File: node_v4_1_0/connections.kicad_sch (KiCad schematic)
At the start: 13 parts, among them J1 Conn_01x02_Pin, J4 Conn_02x08_Odd_Even, J5 Conn_02x02_Odd_Even, J6 GNSS_ANT, J7 RF_ANT, J8 Conn_01x02_Pin

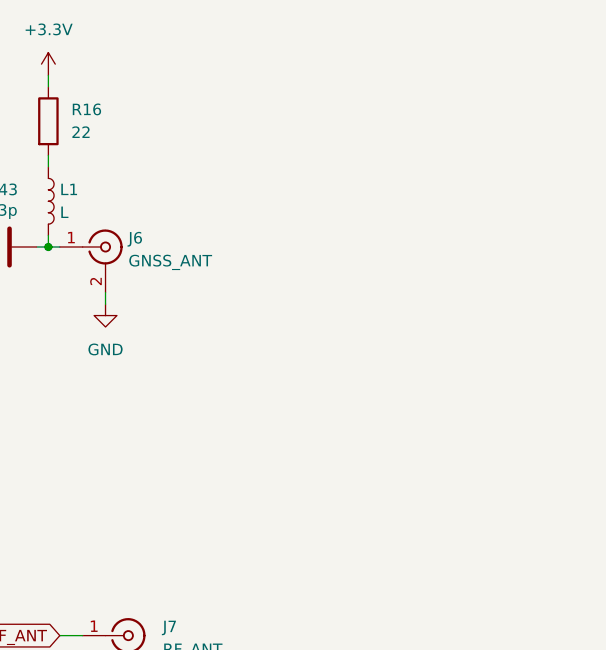
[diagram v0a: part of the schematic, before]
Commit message: small changes to 4.1.1 routing
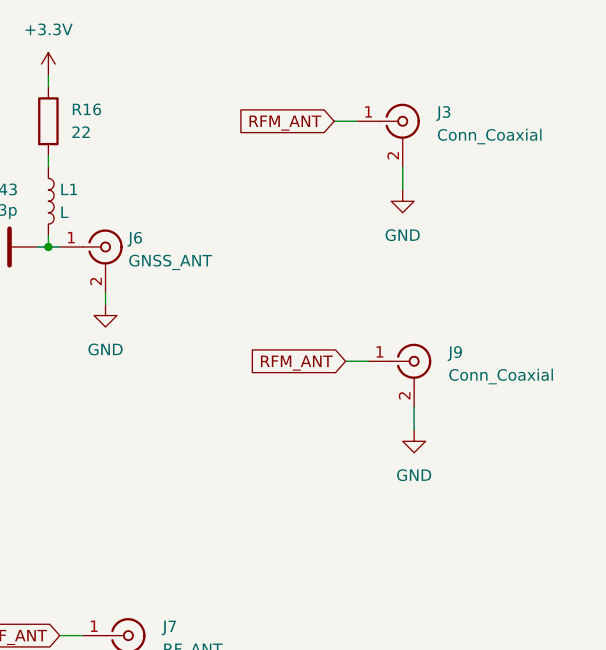
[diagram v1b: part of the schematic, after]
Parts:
- added J3: Conn_Coaxial, Connector_Coaxial:SMA_Samtec_SMA-J-P-H-ST-EM1_EdgeMount, symbol Connector:Conn_Coaxial
- added J9: Conn_Coaxial, WiSDOM:CONN_CONMHF1-SMD_LNX, symbol Connector:Conn_Coaxial
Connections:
- net GND: now also J3.2 (Ext), J9.2 (Ext)
- new net RFM_ANT: J3.1 (In), J9.1 (In)
